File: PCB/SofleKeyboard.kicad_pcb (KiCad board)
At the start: 2 copper layers, 143.5 x 115.5 mm, 85 parts, among them J1 LED, J2 4PIN, J3 OLED, SW1 SW_PUSH, SW10 SW_PUSH, SW11 SW_PUSH, SW12 SW_PUSH, SW13 SW_PUSH, SW14 SW_PUSH, SW15 SW_PUSH, SW16 SW_PUSH, SW17 SW_PUSH, SW18 SW_PUSH, SW19 SW_PUSH, SW2 SW_PUSH, SW20 SW_PUSH, SW21 SW_PUSH, SW22 SW_PUSH, SW23 SW_PUSH, SW24 SW_PUSH, SW25 Rotary_Encoder_Switch, SW26 SW_PUSH, SW27 SW_PUSH, SW28 SW_PUSH, SW29 SW_PUSH, SW3 SW_PUSH, SW30 SW_PUSH, SW4 SW_PUSH, SW5 SW_PUSH, SW6 SW_PUSH, SW7 SW_PUSH, SW8 SW_PUSH, SW9 SW_PUSH, U1 ProMicro

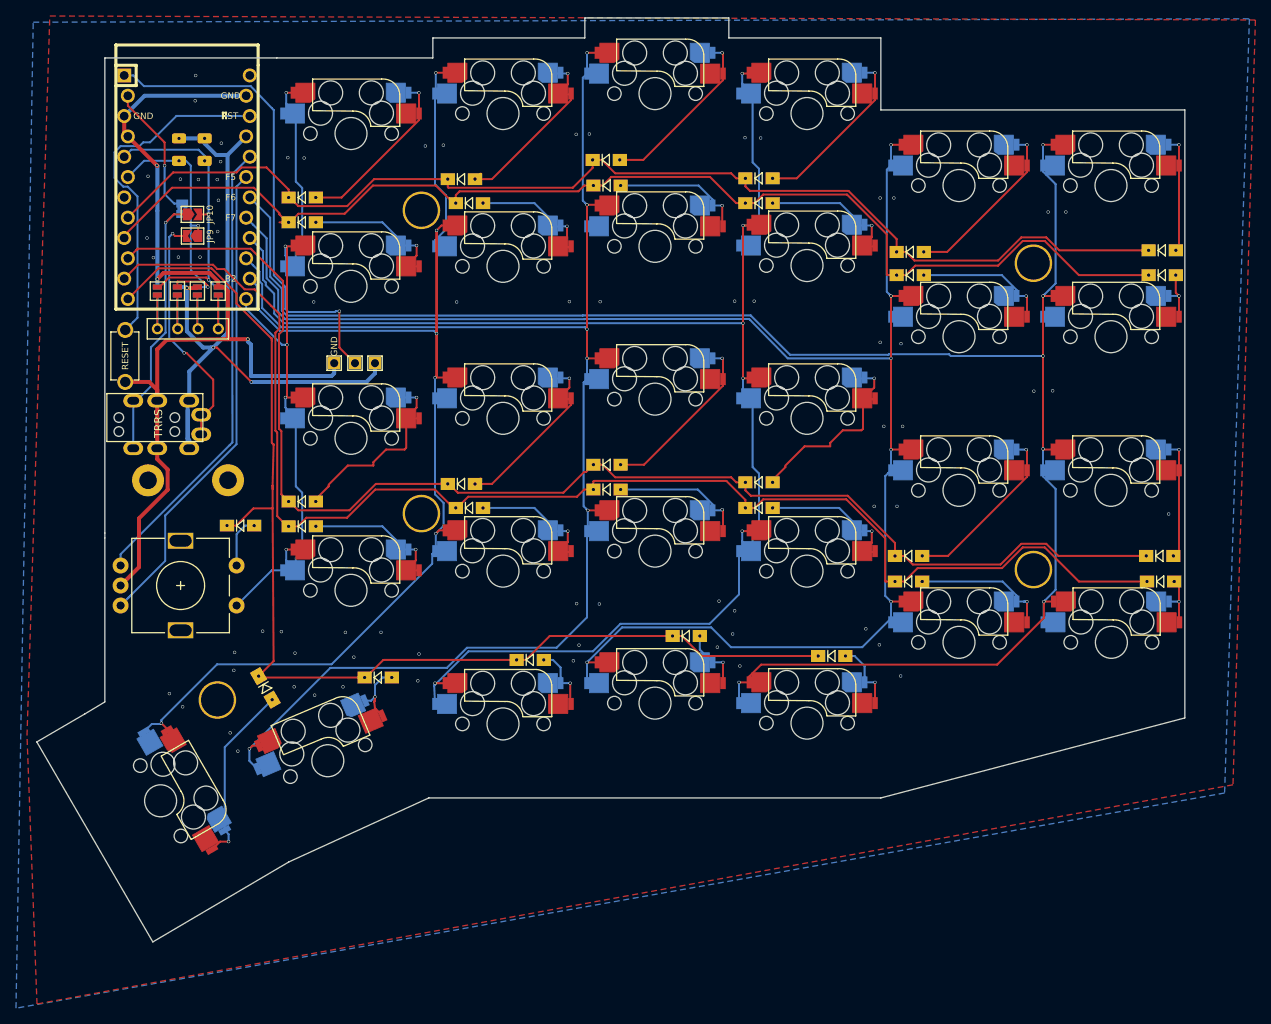
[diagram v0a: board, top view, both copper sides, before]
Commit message: Add logos and credits on all boards
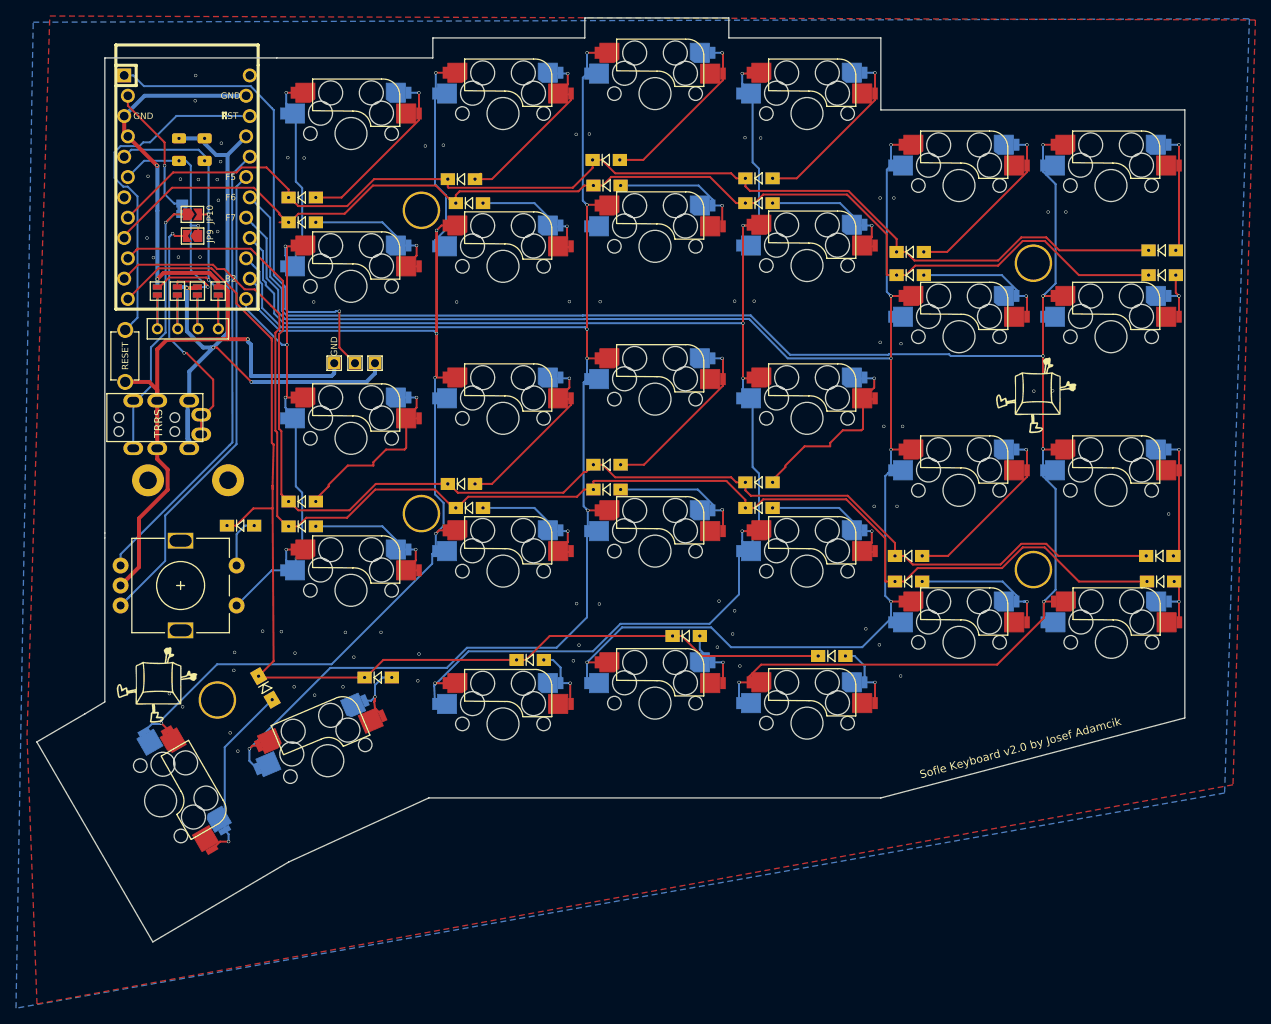
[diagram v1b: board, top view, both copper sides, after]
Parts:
- added Ref**: Val**, SofleKeyboard-footprint:SofleLogoSmall, B.Cu at (205.3, 89.8)
- added Ref**: Val**, SofleKeyboard-footprint:SofleLogoSmall, F.Cu at (206.8, 89.8)
- added Ref**: Val**, SofleKeyboard-footprint:SofleLogoSmall, B.Cu at (95.2, 125.9)
- added Ref**: Val**, SofleKeyboard-footprint:SofleLogoSmall, F.Cu at (96.9, 126.0)
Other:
- board text added: "Sofle Keyboard v2.0 by Josef Adamcik"

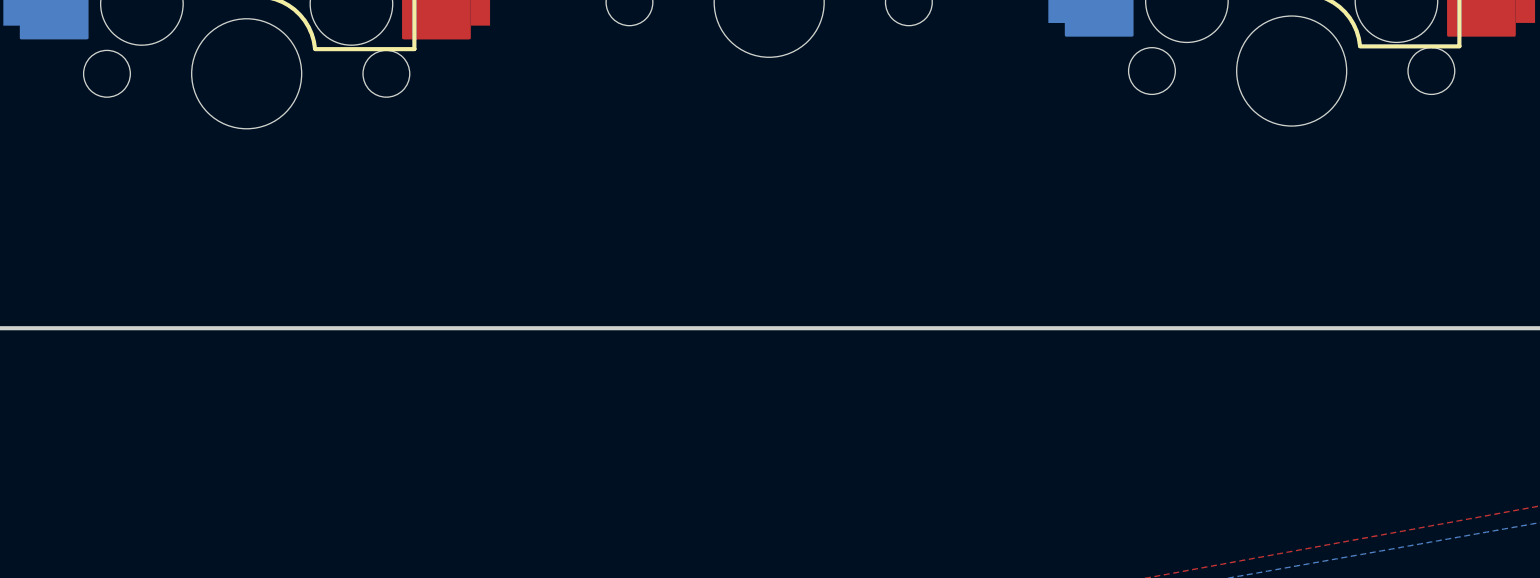
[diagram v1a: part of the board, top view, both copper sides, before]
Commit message: Small improvements to plates
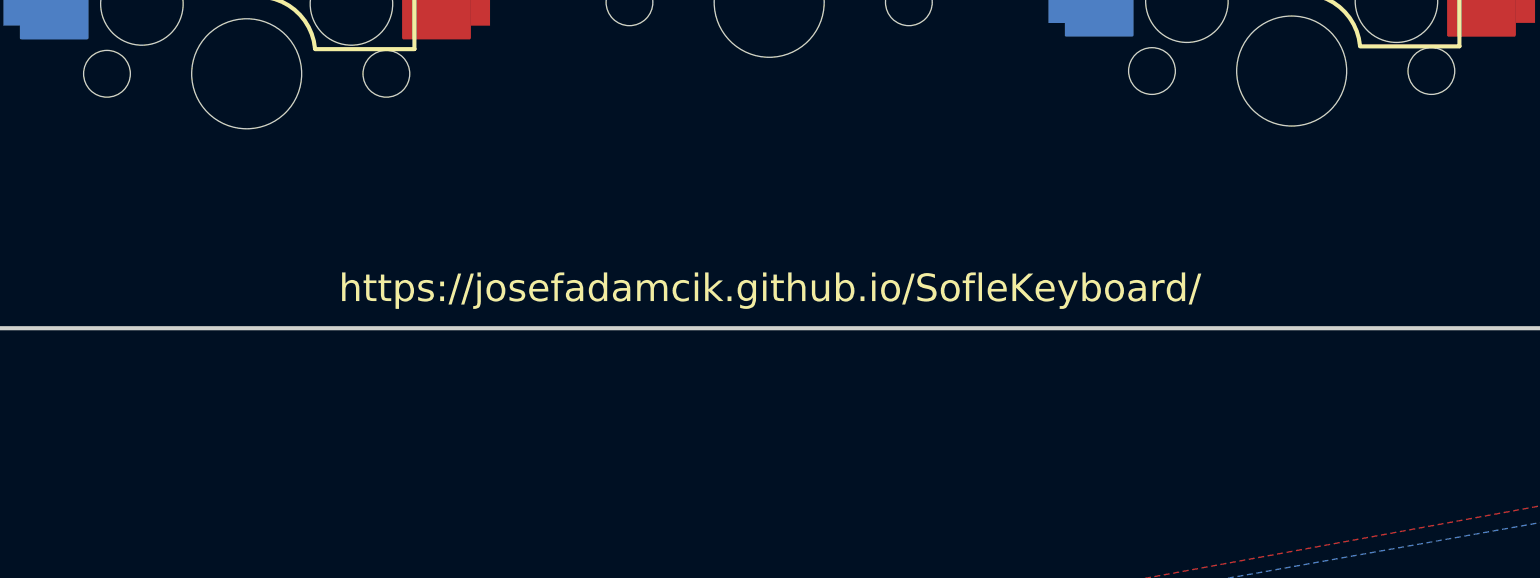
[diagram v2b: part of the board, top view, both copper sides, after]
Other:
- board text added: "https://josefadamcik.github.io/SofleKeyboard/"
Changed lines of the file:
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@@
   (general
     (thickness 1.6)
-    (drawings 28)
+    (drawings 30)
     (tracks 1091)
     (zones 0)
@@
       (net 34 GND))
   )
+  (gr_text https://josefadamcik.github.io/SofleKeyboard/ (at 158.48 131.602) (layer B.SilkS)
+    (effects (font (size 1 1) (thickness 0.15)) (justify mirror))
+  )
+  (gr_text https://josefadamcik.github.io/SofleKeyboard/ (at 158.53 131.602) (layer F.SilkS)
+    (effects (font (size 1 1) (thickness 0.15)))
+  )
   (gr_text "Sofle Keyboard v2.0 by Josef Adamcik" (at 203.93 126.852 15) (layer B.SilkS)
